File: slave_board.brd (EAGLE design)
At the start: 200 x 100 mm, 157 parts, among them IC3 ATMEGA2560-16AU, J1 OSTVN08A150, J11 1935161, J12 OSTVN06A150, J13 OSTVN08A150, J17 RJ45, J18 OSTVN08A150, J2 OSTVN08A150, J22 RJ45, J3 1935161, J4 OSTVN06A150, J6 1935161, J8 OSTVN08A150, K1 ORWH-SH-112D1F, Q1 PHB45NQ15T, Q2 PHB45NQ15T, Q3 BSS138L, Q5 BSS138L, Q7 PHB45NQ15T, Q8 IRFR9024TRPBF, U1 VNQ5E160KTR-E, U2 PCA9615, U3 INA213AIDCKT, U4 VNH7070ASTR, U5 VNH7070ASTR, U6 VNQ5E160KTR-E, U7 INA213AIDCKT, U8 LM340MP-5.0/NOPB, U9 LM340MP-5.0/NOPB, Y1 ABLS-16.000MHZ-B4-T

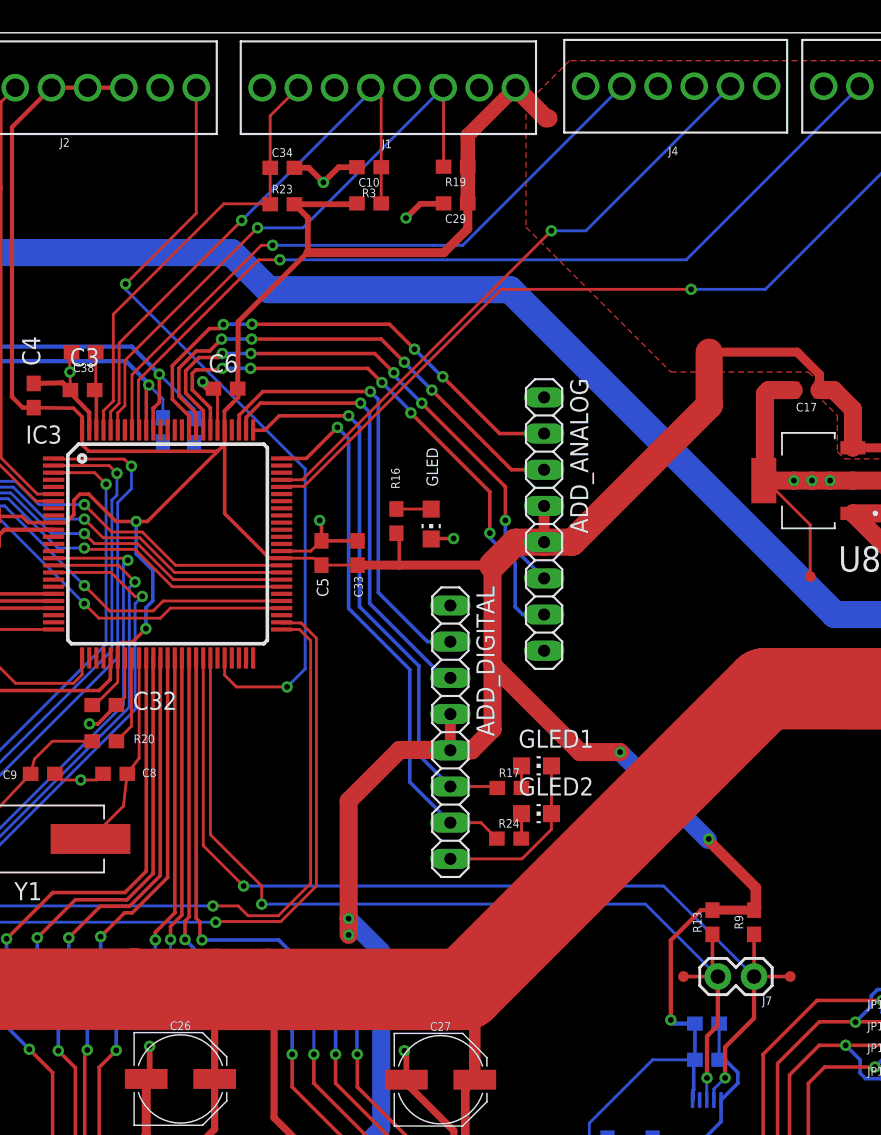
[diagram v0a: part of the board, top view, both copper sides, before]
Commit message: mapped additional elevator encoder input
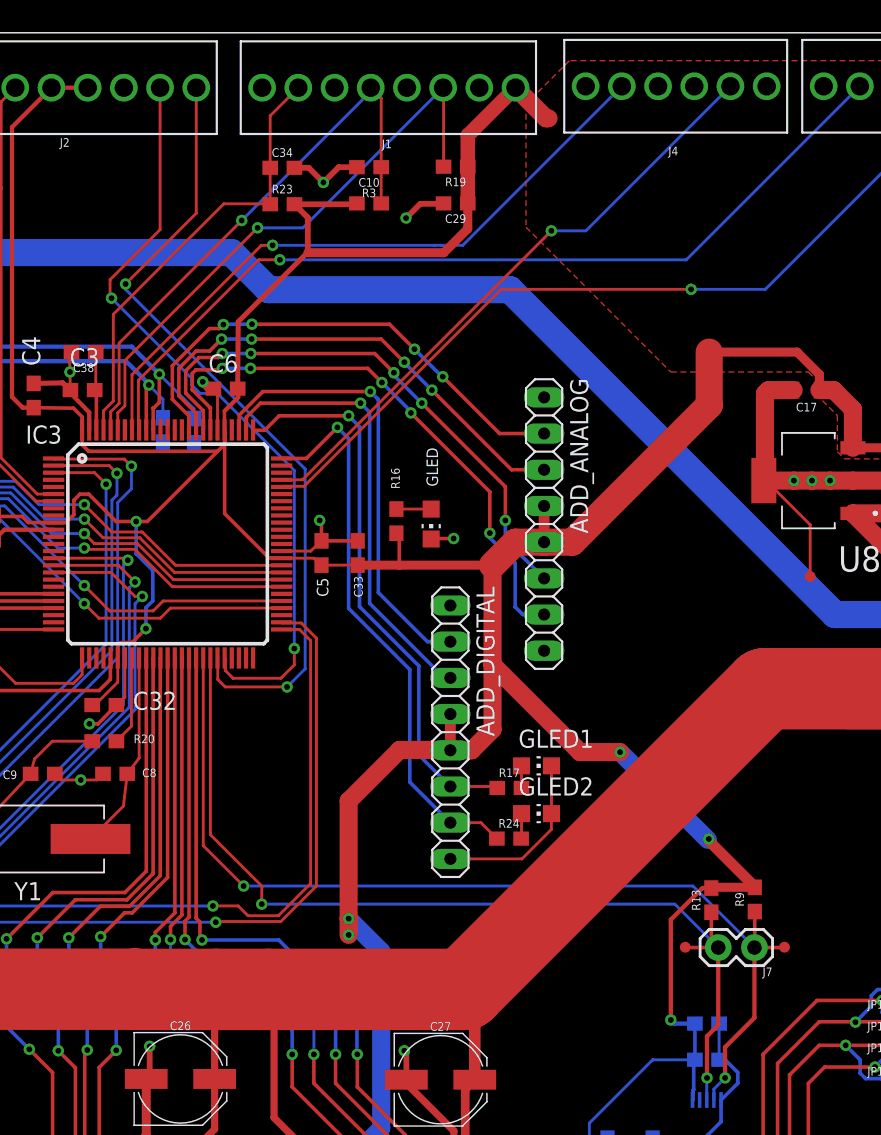
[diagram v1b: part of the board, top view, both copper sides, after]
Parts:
- moved TP14 2.10 mm to (171.6, 35.8)
- moved TP15 2.06 mm to (164.6, 35.8)
- moved J7 2.03 mm to (169.4, 35.8)
- moved R9 1.60 mm to (169.5, 39.2)
- moved R13 1.55 mm to (166.4, 39.1)
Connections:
- removed net ELEV_ENC_OUT: IC3.46, J2.8
- new net ELEV_ENC_A: IC3.45, J2.8
- new net ELEV_ENC_B: IC3.46, J2.7
- net +5V: no longer J2.6
- net GND: now also J2.6; no longer J2.7
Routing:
- net ELEV_ENC_A: track 0.00 -> 56.4 mm, vias 0 -> 2
- net ELEV_ENC_OUT: track 55.8 -> 0.00 mm, vias 2 -> 0
- net ELEV_ENC_B: track 0.00 -> 54.4 mm, vias 0 -> 2
- net +5V: track 418.7 -> 416.0 mm
- net SDA: track 67.4 -> 68.1 mm

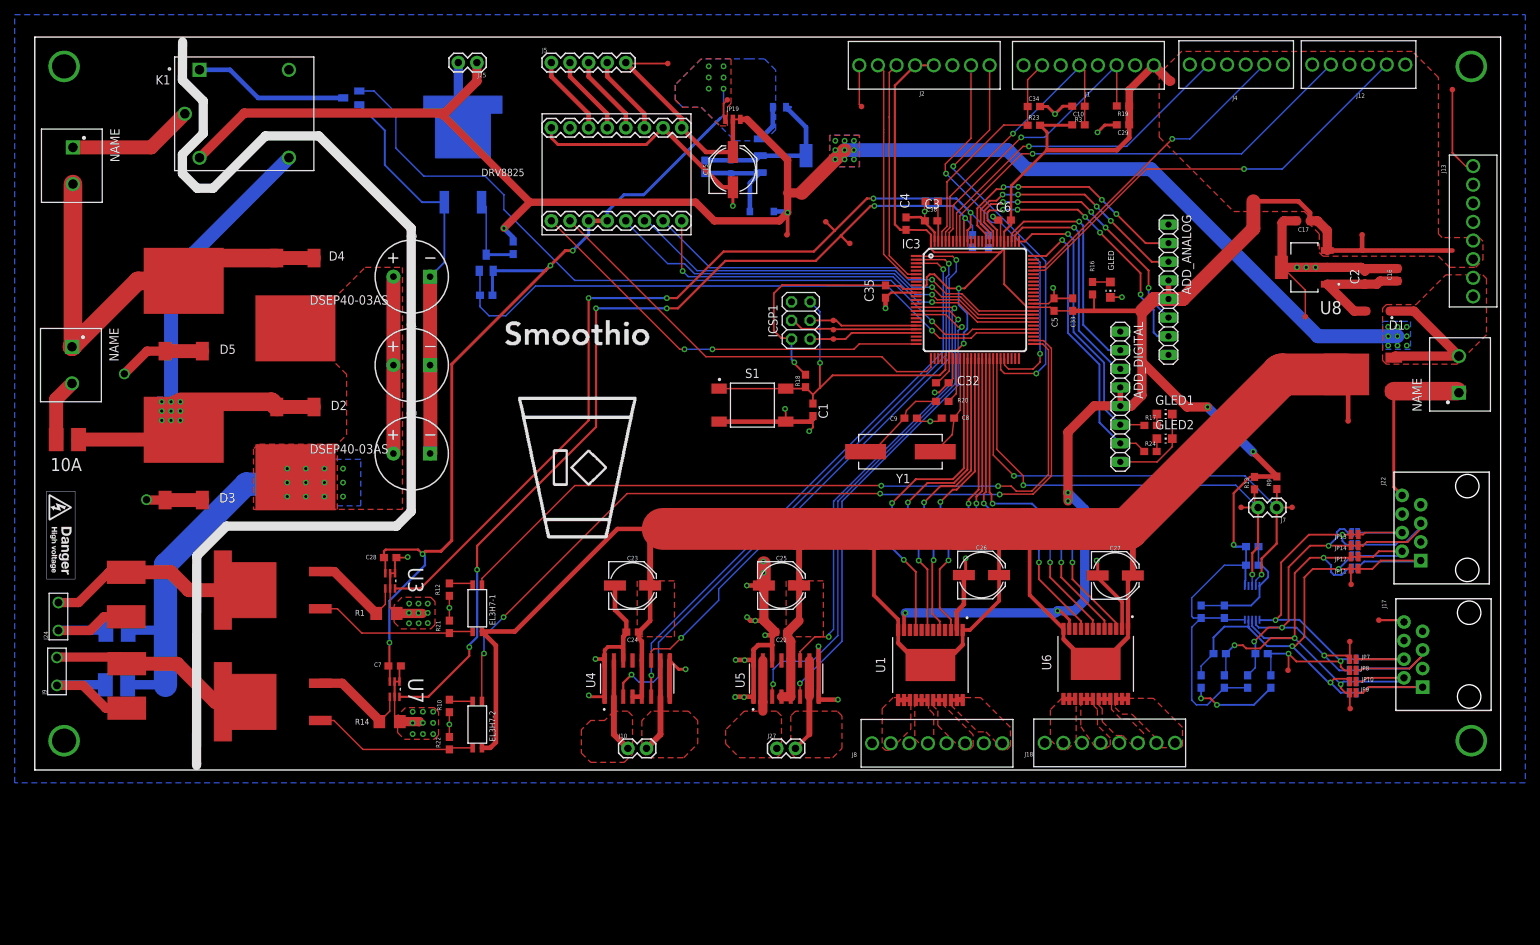
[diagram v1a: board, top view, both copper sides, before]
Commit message: Moved uc pins; fixed all DRCs
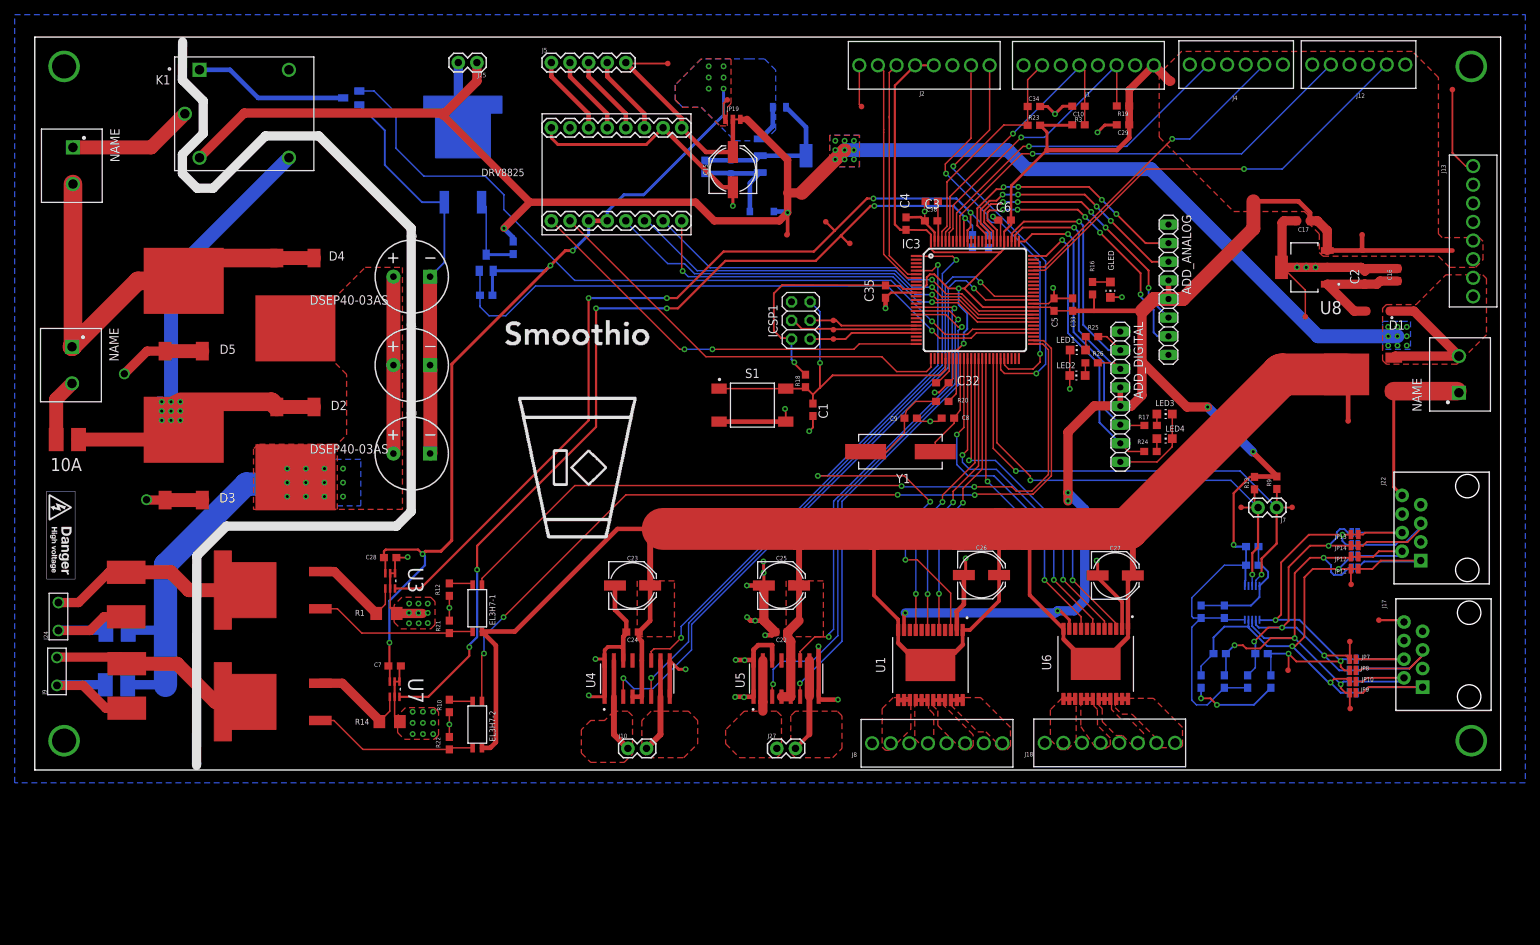
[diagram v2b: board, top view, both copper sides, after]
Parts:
- added LED1, LED2: GREEN, led:CHIP-LED0805
- added R25, R26: 1k, SparkFun-Resistors:0603
- renumbered GLED1 to LED3, GLED2 to LED4
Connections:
- new net N$10: LED2.A, R26.2
- new net N$9: LED1.A, R25.2
- net ADD_D22: now also R25.1
- net ADD_D23: now also R26.1
- net FROZEN1_EN: now also IC3.5; no longer IC3.38
- net FROZEN2_EN: now also IC3.40; no longer IC3.37
- net FROZEN3_EN: now also IC3.39; no longer IC3.36
- net FROZEN4_EN: now also IC3.38; no longer IC3.35
- net GND: now also LED1.C, LED2.C
- net LIQUID1_EN: now also IC3.37; no longer IC3.42
- net LIQUID2_EN: now also IC3.36; no longer IC3.41
- net LIQUID3_EN: now also IC3.35; no longer IC3.40
- net PIVOT_INA: now also IC3.63; no longer IC3.2
- net PIVOT_INB: now also IC3.64; no longer IC3.3
- net POWDER1_EN: now also IC3.41; no longer IC3.39
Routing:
- net FROZEN1_EN: track 40.9 -> 78.8 mm, vias 2 -> 4
- net GND: track 452.7 -> 438.9 mm, vias 61 -> 62
- net PIVOT_INB: track 78.9 -> 86.5 mm
- net PIVOT_INA: track 85.3 -> 91.6 mm
- net FROZEN4_EN: track 45.4 -> 40.4 mm
- net POWDER1_EN: track 46.7 -> 42.3 mm
- net ADD_D22: track 31.7 -> 35.5 mm
- net FROZEN3_EN: track 43.6 -> 39.9 mm
- net ADD_D23: track 31.5 -> 34.9 mm
- net M+: track 82.6 -> 79.9 mm
- net V-5_LOAD: track 135.8 -> 133.3 mm
- net FROZEN2_EN: track 42.0 -> 39.5 mm
- net N$9: track 0.00 -> 1.84 mm
- net N$10: track 0.00 -> 1.74 mm
- net N$13: track 12.9 -> 14.0 mm
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
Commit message: broke blender enable to terminal blocks
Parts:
- added J14, J15: (no value), SparkFun-Connectors:1X02
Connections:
- net BLENDER0_EN: now also J14.1
- net BLENDER1_EN: now also J14.2
- net CURR_SENS0: now also J15.1
- net CURR_SENS1: now also J15.2
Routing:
- net BLENDER0_EN: track 104.1 -> 130.9 mm, vias 2 -> 3
- net BLENDER1_EN: track 115.9 -> 131.5 mm
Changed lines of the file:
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@@
 <rectangle x1="80.4291" y1="60.6171" x2="80.9625" y2="60.6933" layer="21"/>
 <rectangle x1="64.3509" y1="60.6933" x2="66.1797" y2="60.7695" layer="21"/>
-<rectangle x1="76.3905" y1="60.6933" x2="76.8477" y2="60.7695" layer="21"/>
 <rectangle x1="77.9145" y1="60.6933" x2="78.4479" y2="60.7695" layer="21"/>
 <rectangle x1="80.4291" y1="60.6933" x2="81.0387" y2="60.7695" layer="21"/>
@@
 <attribute name="VALUE" x="144.1958" y="56.3118" size="0.6096" layer="27" font="vector" ratio="20" rot="R180" align="top-center"/>
 </element>
+<element name="J14" library="SparkFun-Connectors" library_urn="urn:adsk.eagle:library:513" package="1X02" package3d_urn="urn:adsk.eagle:package:38039/1" value="" x="69.5452" y="2.9464" smashed="yes" rot="R180">
+<attribute name="NAME" x="70.8152" y="1.5494" size="0.6096" layer="25" font="vector" ratio="20" rot="R180"/>
+<attribute name="VALUE" x="70.8152" y="4.9784" size="0.6096" layer="27" font="vector" ratio="20" rot="R180"/>
+</element>
+<element name="J15" library="SparkFun-Connectors" library_urn="urn:adsk.eagle:library:513" package="1X02" package3d_urn="urn:adsk.eagle:package:38039/1" value="" x="76.6064" y="57.785" smashed="yes" rot="R180">
+<attribute name="NAME" x="77.8764" y="56.388" size="0.6096" layer="25" font="vector" ratio="20" rot="R180"/>
+<attribute name="VALUE" x="77.8764" y="59.817" size="0.6096" layer="27" font="vector" ratio="20" rot="R180"/>
+</element>
 </elements>
 <signals>
@@
 <vertex x="124.9934" y="8.8646"/>
 <vertex x="128.6574" y="5.2006"/>
-<vertex x="129.7734" y="5.2006"/>
-<vertex x="131.0894" y="3.8846"/>
+<vertex x="130.0782" y="5.2006"/>
+<vertex x="131.0894" y="4.1894"/>
 <vertex x="131.0894" y="3.2766"/>
 <vertex x="131.5974" y="2.7686"/>
@@
 <vertex x="122.4534" y="8.8646"/>
 <vertex x="123.2154" y="8.1026"/>
-<vertex x="123.2154" y="6.0706"/>
-<vertex x="126.5174" y="2.7686"/>
-<vertex x="127.5254" y="2.7686"/>
-<vertex x="128.0334" y="3.2766"/>
-<vertex x="128.0334" y="4.8086"/>
+<vertex x="123.2154" y="6.723"/>
+<vertex x="126.9031" y="3.0353"/>
+<vertex x="127.8048" y="3.937"/>
+<vertex x="127.8048" y="5.0372"/>
 <vertex x="123.9774" y="8.8646"/>
 <vertex x="123.9774" y="9.3726"/>
@@
 <wire x1="120.9994" y1="9.5456" x2="121.7994" y2="9.5456" width="0.508" layer="1"/>
 <polygon width="0.254" layer="1" thermals="no">
-<vertex x="120.0674" y="9.3726"/>
-<vertex x="120.0674" y="4.2656"/>
-<vertex x="121.5644" y="2.7686"/>
-<vertex x="121.9454" y="2.7686"/>
-<vertex x="122.6534" y="3.4766"/>
+<vertex x="120.0928" y="9.3726"/>
+<vertex x="120.0928" y="4.8244"/>
+<vertex x="121.7676" y="3.1496"/>
+<vertex x="122.6534" y="4.0354"/>
 <vertex x="122.6534" y="7.6486"/>
 <vertex x="121.9454" y="8.3566"/>
@@
 <vertex x="119.3419" y="9.8806"/>
 <vertex x="117.1194" y="9.8806"/>
-<vertex x="115.6144" y="8.3756"/>
-<vertex x="115.6144" y="3.1306"/>
-<vertex x="116.0494" y="2.6956"/>
-<vertex x="116.6654" y="2.6956"/>
-<vertex x="119.5324" y="5.5626"/>
+<vertex x="115.9446" y="8.7058"/>
+<vertex x="115.9446" y="3.2132"/>
+<vertex x="116.4495" y="2.7083"/>
+<vertex x="119.5324" y="5.7912"/>
 <vertex x="119.5324" y="9.4996"/>
 </polygon>
@@
 <vertex x="147.4216" y="8.509"/>
 <vertex x="148.3106" y="7.62"/>
-<vertex x="149.7076" y="7.62"/>
-<vertex x="153.6446" y="3.683"/>
-<vertex x="153.6446" y="3.048"/>
-<vertex x="156.3146" y="3.048"/>
+<vertex x="151.3586" y="7.62"/>
+<vertex x="154.7622" y="4.2164"/>
+<vertex x="154.7622" y="2.9718"/>
+<vertex x="156.2384" y="2.9718"/>
 <vertex x="156.5956" y="3.329"/>
 <vertex x="156.5956" y="5.812"/>
@@
 <polygon width="0.254" layer="1" thermals="no">
 <vertex x="142.7226" y="9.525"/>
-<vertex x="142.7226" y="5.92080625"/>
-<vertex x="144.85603125" y="2.884496875"/>
+<vertex x="142.7226" y="6.4386"/>
+<vertex x="145.219853125" y="2.884496875"/>
 <vertex x="145.965503125" y="2.884496875"/>
-<vertex x="146.7358" y="3.360340625"/>
-<vertex x="146.7358" y="4.3642"/>
+<vertex x="146.4818" y="3.203434375"/>
+<vertex x="146.4818" y="4.6182"/>
 <vertex x="144.9991875" y="6.1008125"/>
 <vertex x="144.9816" y="8.282"/>
@@
 <vertex x="141.4526" y="9.779"/>
 <vertex x="140.1206" y="9.779"/>
-<vertex x="138.5696" y="8.228"/>
-<vertex x="138.5696" y="4.118"/>
-<vertex x="139.9046" y="2.783"/>
-<vertex x="140.8746" y="2.783"/>
-<vertex x="142.0876" y="3.996"/>
+<vertex x="138.893271875" y="8.551671875"/>
+<vertex x="138.893271875" y="4.510328125"/>
+<vertex x="140.3285" y="3.0751"/>
+<vertex x="142.0876" y="4.8342"/>
 <vertex x="142.0876" y="9.144"/>
 </polygon>
@@
 <vertex x="145.6436" y="8.382"/>
 <vertex x="145.6436" y="6.607"/>
-<vertex x="147.5516" y="4.699"/>
-<vertex x="148.4216" y="4.699"/>
-<vertex x="150.4131" y="2.7075"/>
+<vertex x="146.9674" y="5.2832"/>
+<vertex x="148.4978" y="5.2832"/>
+<vertex x="150.7433" y="3.0377"/>
 <vertex x="151.2886" y="3.583"/>
 <vertex x="151.2886" y="5.023"/>
@@
 <contactref element="U3" pad="6"/>
 <contactref element="IC3" pad="90"/>
-<wire x1="75.565" y1="64.389" x2="75.565" y2="47.7012" width="0.3048" layer="1"/>
+<wire x1="75.565" y1="64.389" x2="74.0664" y2="62.8904" width="0.3048" layer="1"/>
 <via x="75.565" y="64.389" extent="1-16" drill="0.4064"/>
 <wire x1="75.565" y1="64.389" x2="86.233" y2="64.389" width="0.3048" layer="16"/>
@@
 <wire x1="109.1057" y1="73.6219" x2="109.1819" y2="73.6219" width="0.3048" layer="1"/>
 <wire x1="52.6288" y1="24.765" x2="49.149" y2="24.765" width="0.3048" layer="1"/>
-<wire x1="75.565" y1="47.7012" x2="52.6288" y2="24.765" width="0.3048" layer="1"/>
+<wire x1="74.0664" y1="46.2026" x2="52.6288" y2="24.765" width="0.3048" layer="1"/>
+<contactref element="J15" pad="2"/>
+<wire x1="74.0664" y1="62.8904" x2="74.0664" y2="57.785" width="0.3048" layer="1"/>
+<wire x1="74.0664" y1="57.785" x2="74.0664" y2="46.2026" width="0.3048" layer="1"/>
 </signal>
 <signal name="V-HVDC" class="4">
@@
 <contactref element="U7" pad="6"/>
 <contactref element="IC3" pad="91"/>
-<wire x1="76.581" y1="62.992" x2="76.581" y2="46.8122" width="0.3048" layer="1"/>
 <via x="76.581" y="62.992" extent="1-16" drill="0.4064"/>
 <wire x1="76.581" y1="62.992" x2="86.233" y2="62.992" width="0.3048" layer="16"/>
@@
 <wire x1="59.2836" y1="15.5702" x2="53.6956" y2="9.9822" width="0.3048" layer="1"/>
 <wire x1="49.7586" y1="9.9822" x2="53.6956" y2="9.9822" width="0.3048" layer="1"/>
-<wire x1="76.581" y1="46.8122" x2="60.3504" y2="30.5816" width="0.3048" layer="1"/>
+<wire x1="60.3504" y1="30.5816" x2="76.581" y2="46.8122" width="0.3048" layer="1"/>
 <wire x1="60.3504" y1="30.5816" x2="60.3504" y2="27.3304" width="0.3048" layer="1"/>
+<contactref element="J15" pad="1"/>
+<wire x1="76.581" y1="46.8122" x2="76.581" y2="57.7596" width="0.3048" layer="1"/>
+<wire x1="76.581" y1="57.7596" x2="76.6064" y2="57.785" width="0.3048" layer="1"/>
+<wire x1="76.581" y1="62.992" x2="76.581" y2="57.8104" width="0.3048" layer="1"/>
+<wire x1="76.6064" y1="57.785" x2="76.581" y2="57.8104" width="0.3048" layer="1"/>
 </signal>
 <signal name="PIVOT_OUT_A" class="1">
@@
 <wire x1="117.729" y1="37.5158" x2="117.729" y2="37.5412" width="0.2032" layer="16"/>
 <via x="117.729" y="37.5412" extent="1-16" drill="0.4064"/>
-<wire x1="117.729" y1="37.5412" x2="80.645" y2="37.5412" width="0.2032" layer="1"/>
-<wire x1="80.645" y1="37.5412" x2="63.9572" y2="20.8534" width="0.2032" layer="1"/>
-<via x="63.9572" y="20.8534" extent="1-16" drill="0.4064"/>
-<wire x1="63.9572" y1="20.8534" x2="61.2902" y2="18.1864" width="0.2032" layer="16"/>
-<wire x1="61.2902" y1="18.1864" x2="61.2902" y2="15.9004" width="0.2032" layer="16"/>
+<wire x1="117.729" y1="37.5412" x2="80.01" y2="37.5412" width="0.2032" layer="1"/>
+<wire x1="80.01" y1="37.5412" x2="64.3382" y2="21.8694" width="0.2032" layer="1"/>
+<via x="64.3382" y="21.8694" extent="1-16" drill="0.4064"/>
+<wire x1="64.3382" y1="21.8694" x2="63.3984" y2="20.9296" width="0.2032" layer="16"/>
+<wire x1="63.3984" y1="20.9296" x2="63.3984" y2="18.0086" width="0.2032" layer="16"/>
+<wire x1="63.3984" y1="18.0086" x2="61.2902" y2="15.9004" width="0.2032" layer="16"/>
 <via x="61.2902" y="15.9004" extent="1-16" drill="0.4064"/>
 <wire x1="61.2902" y1="15.9004" x2="60.9854" y2="15.5956" width="0.2032" layer="1"/>
 <wire x1="60.9854" y1="15.5956" x2="60.9854" y2="9.398" width="0.2032" layer="1"/>
 <wire x1="61.0108" y1="9.3726" x2="60.9854" y2="9.398" width="0.2032" layer="1"/>
+<contactref element="J14" pad="2"/>
+<wire x1="61.2902" y1="15.9004" x2="67.0052" y2="10.1854" width="0.2032" layer="16"/>
+<wire x1="67.0052" y1="10.1854" x2="67.0052" y2="2.9464" width="0.2032" layer="16"/>
 </signal>
 <signal name="BLENDER0_EN">
@@
 <wire x1="73.6854" y1="38.8112" x2="61.0108" y2="26.1366" width="0.2032" layer="1"/>
 <wire x1="61.0108" y1="26.1366" x2="61.0108" y2="25.2476" width="0.2032" layer="1"/>
+<contactref element="J14" pad="1"/>
+<wire x1="61.0108" y1="25.2476" x2="62.4586" y2="23.7998" width="0.2032" layer="1"/>
+<wire x1="62.4586" y1="23.7998" x2="62.4586" y2="20.7264" width="0.2032" layer="1"/>
+<wire x1="62.4586" y1="20.7264" x2="63.119" y2="20.066" width="0.2032" layer="1"/>
+<wire x1="63.119" y1="20.066" x2="64.7446" y2="20.066" width="0.2032" layer="1"/>
+<via x="64.7446" y="20.066" extent="1-16" drill="0.4064"/>
+<wire x1="64.7446" y1="20.066" x2="64.7446" y2="14.5542" width="0.2032" layer="16"/>
+<wire x1="69.5452" y1="9.7536" x2="69.5452" y2="2.9464" width="0.2032" layer="16"/>
+<wire x1="64.7446" y1="14.5542" x2="69.5452" y2="9.7536" width="0.2032" layer="16"/>
 </signal>
 <signal name="COOLANT_EN">
